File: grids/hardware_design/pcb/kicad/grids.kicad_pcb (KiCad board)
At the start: 2 copper layers, 78.1 x 102.9 mm, 107 parts, among them IC1 ATMEGA328P-AU, IC2 LM4040 5.0V, IC3 MCP6002, IC4 MCP6002, IC5 MCP6002, IC6 74595D, IC7 LM1117-5.0, J1 PJ301WQP, J10 PJ301WQP, J11 PJ301WQP, J12 PJ301WQP, J13 PJ301WQP, J14 PJ301WQP, J15 AVR_SPI_PRG_6PTH, J16 M05X2PTH, J17 AVR_SPI_PRG_6PTH, J2 PJ301WQP, J3 PJ301WQP, J4 PJ301WQP, J5 PJ301WQP, J6 PJ301WQP, J7 PJ301WQP, J8 PJ301WQP, J9 PJ301WQP, Q1 20MHz, Q2 MMBT3904, Q3 MMBT3904, SW1 SW_MEC_5G_2LED

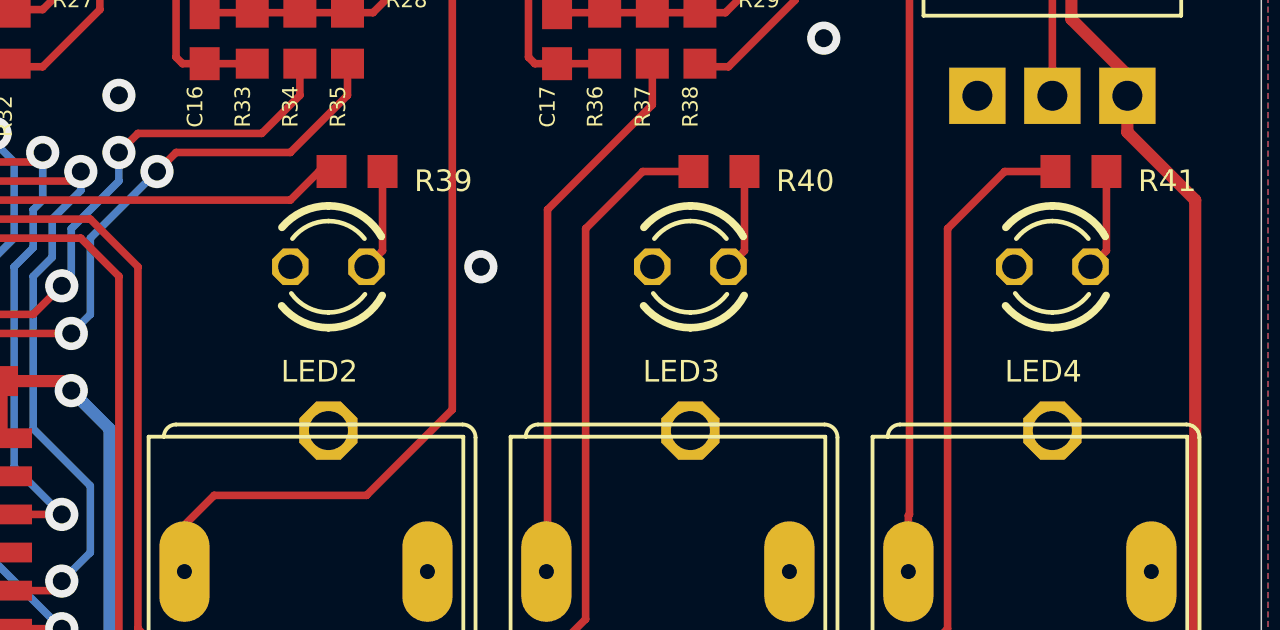
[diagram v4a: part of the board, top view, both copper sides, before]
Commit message: add 0603 LEDs in parallel with other footprint
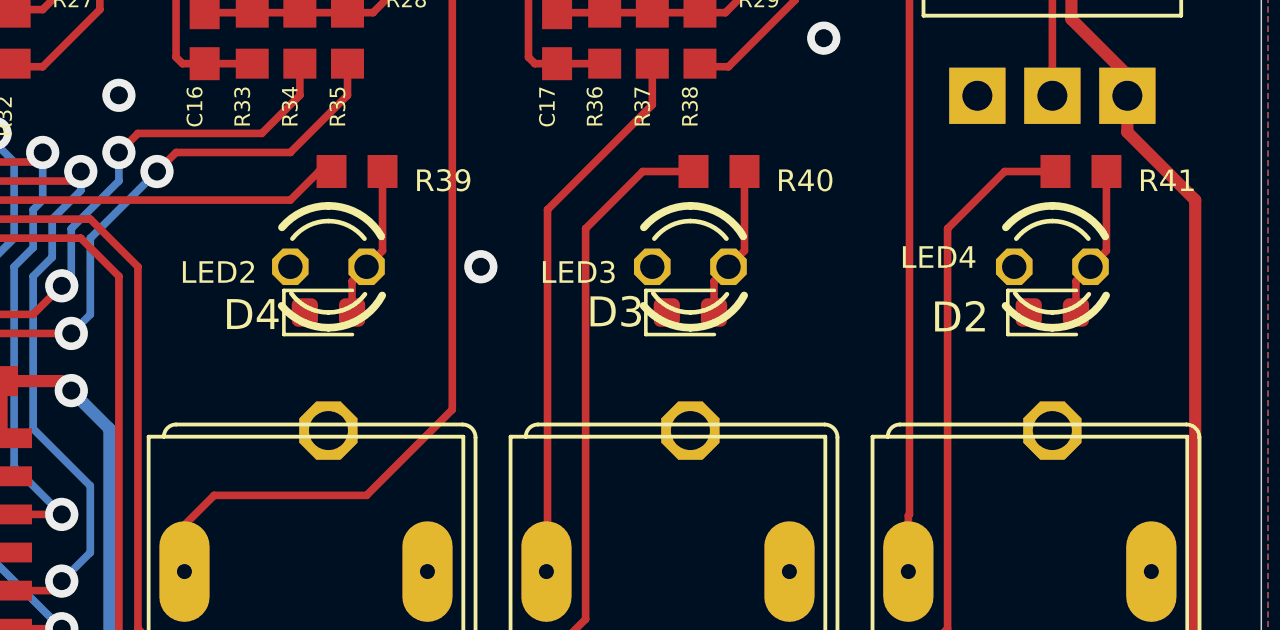
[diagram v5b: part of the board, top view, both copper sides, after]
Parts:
- added D2: LED, LED_SMD:LED_0603_1608Metric, F.Cu at (180.6, 117.3)
- added D3: LED, LED_SMD:LED_0603_1608Metric, F.Cu at (168.5, 117.3)
- added D4: LED, LED_SMD:LED_0603_1608Metric, F.Cu at (156.4, 117.3)
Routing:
- net Net-(R39-Pad2): track 3.40 -> 5.12 mm
- net Net-(R41-Pad2): track 3.40 -> 5.12 mm
- net Net-(R40-Pad2): track 3.40 -> 5.12 mm

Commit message: change the jack again
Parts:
- J1, J10, J11, J12, J13, J14, J2, J3, J4, J5, J6, J7, J8, J9: footprint grids:WQP_PJ_301BM -> marbles:WQP_PJ_301M6
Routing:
- net /LED_CH3: track 109.9 -> 0.00 mm
- net Net-(J7-PadTIP): track 33.9 -> 143.8 mm
- net /RESET: track 98.7 -> 0.00 mm, vias 2 -> 1
- net /MOSI: track 114.5 -> 213.2 mm, vias 4 -> 5
- net Net-(J6-PadTIP): track 18.4 -> 114.8 mm
- net /LED_CH2: track 96.4 -> 0.00 mm
- net Net-(J1-PadTIP): track 36.9 -> 61.1 mm
- net Net-(J2-PadTIP): track 24.1 -> 0.00 mm

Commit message: some random ctrl-s
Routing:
- net /RESET: track 0.00 -> 213.2 mm, vias 1 -> 4
- net /MOSI: track 213.2 -> 0.00 mm, vias 5 -> 2
